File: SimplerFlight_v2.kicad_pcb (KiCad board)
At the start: 2 copper layers, 77 parts, among them J1 Battery 1, J10 Cam 2, J11 Cam 3, J12 Encoder, J13 Servo, J14 DM3CS-SF, J3 USART1 Header, J4 I2C1 Header, J5 SPI Header, J6 SWD Header, J7 Battery 2, J8 USB, J9 Cam 1, SW1 Boot Switch, SW2 System Reset, U1 AMS1117-3.3, U2 STM32F401RETx, U3 BMP581, U4 BNO085, U5 TPS62933, U6 TPS62933, U7 W25X40CLSNIG, Y1 16MHz, Y2 Crystal

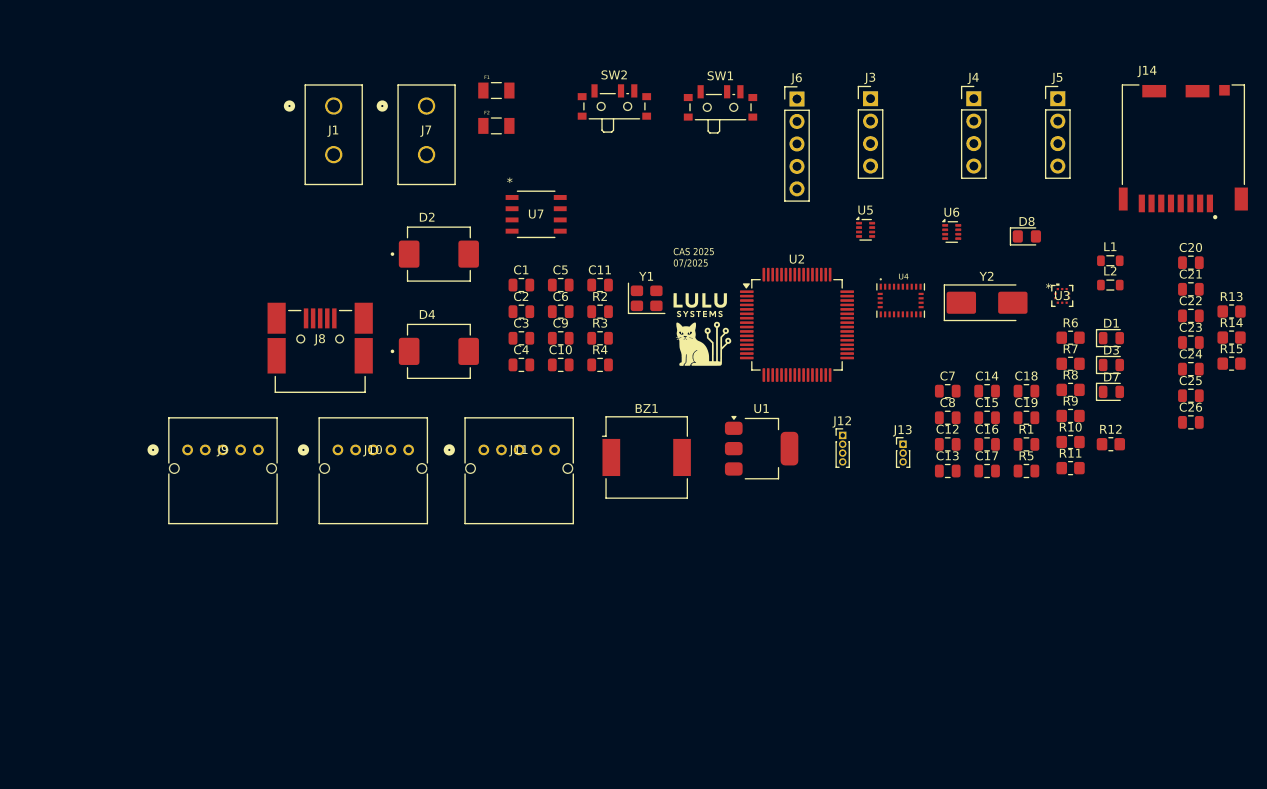
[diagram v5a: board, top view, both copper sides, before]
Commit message: Update schematic, pending power sims, updated README
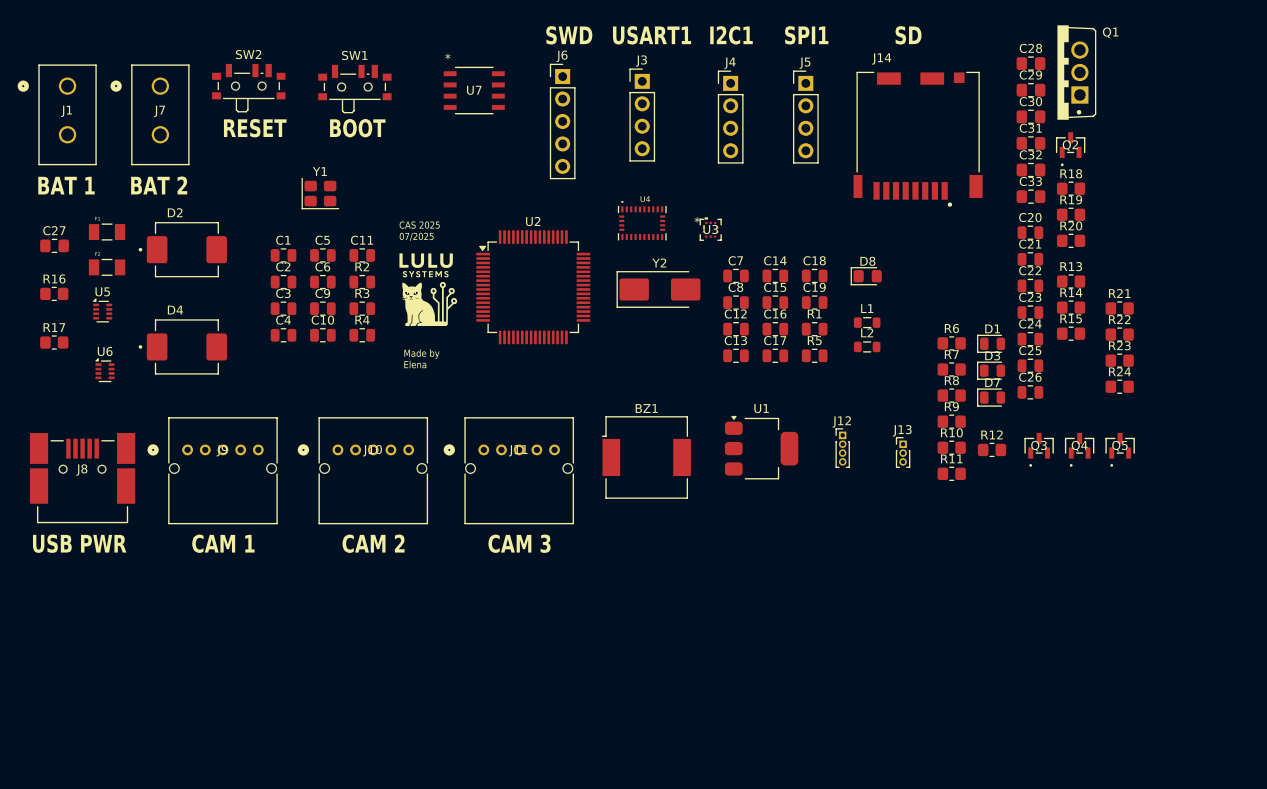
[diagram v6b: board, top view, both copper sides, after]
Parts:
- added C27: 100nF, Capacitor_SMD:C_0805_2012Metric_Pad1.18x1.45mm_HandSolder, F.Cu at (52.0, 40.6)
- added C28: 10uF, Capacitor_SMD:C_0805_2012Metric_Pad1.18x1.45mm_HandSolder, F.Cu at (162.5, 19.9)
- added C29: 100uF, Capacitor_SMD:C_0805_2012Metric_Pad1.18x1.45mm_HandSolder, F.Cu at (162.5, 23.0)
- added C30: 100uF, Capacitor_SMD:C_0805_2012Metric_Pad1.18x1.45mm_HandSolder, F.Cu at (162.5, 26.0)
- added C31: 10uF, Capacitor_SMD:C_0805_2012Metric_Pad1.18x1.45mm_HandSolder, F.Cu at (162.5, 29.0)
- added C32: 100uF, Capacitor_SMD:C_0805_2012Metric_Pad1.18x1.45mm_HandSolder, F.Cu at (162.5, 32.0)
- added C33: 10uF, Capacitor_SMD:C_0805_2012Metric_Pad1.18x1.45mm_HandSolder, F.Cu at (162.5, 35.0)
- added Q1: IRF520NPBF, IRF520NPBF:TO-220-3, F.Cu at (168.0, 21.0)
- added Q2: NPN, FSB560A:SSOT3_3X1P5_ONS, F.Cu at (167.0, 29.2)
- added Q3: NPN, FSB560A:SSOT3_3X1P5_ONS, F.Cu at (163.4, 63.2)
- added Q4: NPN, FSB560A:SSOT3_3X1P5_ONS, F.Cu at (168.0, 63.2)
- added Q5: NPN, FSB560A:SSOT3_3X1P5_ONS, F.Cu at (172.5, 63.2)
- added R16: 10k, Resistor_SMD:R_0805_2012Metric_Pad1.20x1.40mm_HandSolder, F.Cu at (52.0, 46.0)
- added R17: 10k, Resistor_SMD:R_0805_2012Metric_Pad1.20x1.40mm_HandSolder, F.Cu at (52.0, 51.5)
- added R18: 10K, Resistor_SMD:R_0805_2012Metric_Pad1.20x1.40mm_HandSolder, F.Cu at (167.0, 34.1)
- added R19: 10k, Resistor_SMD:R_0805_2012Metric_Pad1.20x1.40mm_HandSolder, F.Cu at (167.0, 37.0)
- added R20: 470, Resistor_SMD:R_0805_2012Metric_Pad1.20x1.40mm_HandSolder, F.Cu at (167.0, 40.0)
- added R21: R, Resistor_SMD:R_0805_2012Metric_Pad1.20x1.40mm_HandSolder, F.Cu at (172.5, 47.6)
- added R22: R, Resistor_SMD:R_0805_2012Metric_Pad1.20x1.40mm_HandSolder, F.Cu at (172.5, 50.6)
- added R23: R, Resistor_SMD:R_0805_2012Metric_Pad1.20x1.40mm_HandSolder, F.Cu at (172.5, 53.5)
- added R24: R, Resistor_SMD:R_0805_2012Metric_Pad1.20x1.40mm_HandSolder, F.Cu at (172.5, 56.5)
- moved U6 97.0 mm to (57.7, 54.8)
- moved U5 86.8 mm to (57.5, 48.0)
- moved F1 46.8 mm to (58.0, 39.0)
- moved F2 46.8 mm to (58.0, 43.0)
- moved SW1 41.4 mm to (86.0, 22.3)
- moved SW2 41.4 mm to (74.0, 22.2)
- moved U3 40.5 mm to (126.2, 38.8)
- moved Y1 38.8 mm to (82.1, 34.6)
- moved Y2 37.0 mm to (120.5, 45.5)
- moved G*** 31.3 mm to (94.0, 45.5)
- moved J8 30.6 mm to (55.2, 65.8)
- moved U4 30.5 mm to (118.5, 38.0)
- moved J1 30.2 mm to (53.5, 22.5)
- moved J7 30.2 mm to (64.0, 22.5)
- moved U2 30.1 mm to (106.2, 45.2)
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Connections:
- net Net-(D8-A) renamed /Power/VBUS_CAM
- net Net-(D8-K) renamed /Power/VBUS_USB
- net Net-(U5-VIN) renamed /Power/VBUS_SERVO
- BZ1 pad 1: unconnected-(BZ1-+-Pad1) -> +3V3
- BZ1 pad 2: unconnected-(BZ1---Pad2) -> Net-(BZ1--)
- J10 pad 1: unconnected-(J10-Pad1) -> Net-(Q4-E)
- J10 pad 2: unconnected-(J10-Pad2) -> GND
- J10 pad 3: unconnected-(J10-Pad3) -> CAM2_RX
- J10 pad 4: unconnected-(J10-Pad4) -> CAM2_TX
- J11 pad 1: unconnected-(J11-Pad1) -> Net-(Q3-E)
- J11 pad 2: unconnected-(J11-Pad2) -> GND
- J11 pad 3: unconnected-(J11-Pad3) -> CAM3_RX
- J11 pad 4: unconnected-(J11-Pad4) -> CAM3_TX
- J12 pad 1: unconnected-(J12-Pin_1-Pad1) -> 5V_SERVO
- J12 pad 2: unconnected-(J12-Pin_2-Pad2) -> GND
- J12 pad 3: unconnected-(J12-Pin_3-Pad3) -> ENC_A
- J12 pad 4: unconnected-(J12-Pin_4-Pad4) -> ENC_B
- J13 pad 1: unconnected-(J13-Pin_1-Pad1) -> SERVO_PWM
- J13 pad 2: unconnected-(J13-Pin_2-Pad2) -> Net-(J13-Pin_2)
- J13 pad 3: unconnected-(J13-Pin_3-Pad3) -> GND
- J14 pad 2: unconnected-(J14-CD/DAT3-Pad2) -> CS
- J14 pad 3: unconnected-(J14-CMD-Pad3) -> SI
- J14 pad 4: unconnected-(J14-VDD-Pad4) -> +3V3
- J14 pad 5: unconnected-(J14-CLK-Pad5) -> SCK
- J14 pad 6: unconnected-(J14-VSS-Pad6) -> GND
- J14 pad 7: unconnected-(J14-DAT0-Pad7) -> SO
- J14 pad 9: unconnected-(J14-CD_SW-Pad9) -> C_DET
- J14 pad S1: unconnected-(J14-GND-PadS1) -> GND
- J14 pad S2: unconnected-(J14-GND__1-PadS2) -> GND
- J14 pad S3: unconnected-(J14-GND__2-PadS3) -> GND
- J14 pad S5: unconnected-(J14-GND__3-PadS5) -> GND
- J8 pad 2: /Power/USB_OTG_FS_D- -> USB_DN
- J8 pad 3: /Power/USB_OTG_FS_D+ -> USB_DP
- J9 pad 1: unconnected-(J9-Pad1) -> Net-(Q5-E)
- J9 pad 2: unconnected-(J9-Pad2) -> GND
- J9 pad 3: unconnected-(J9-Pad3) -> CAM1_RX
- J9 pad 4: unconnected-(J9-Pad4) -> CAM1_TX
- U2 pad 44: /Microcontroller/USB_OTG_FS_D- -> USB_DN
- U2 pad 45: /Microcontroller/USB_OTG_FS_D+ -> USB_DP
- U5 pad 2: unconnected-(U5-EN-Pad2) -> Net-(U5-EN)
- U5 pad 4: unconnected-(U5-GND-Pad4) -> GND
- U6 pad 2: unconnected-(U6-EN-Pad2) -> Net-(U6-EN)
- U6 pad 4: unconnected-(U6-GND-Pad4) -> GND
- U7 pad 4: unconnected-(U7-GND-Pad4) -> GND
- U7 pad 8: unconnected-(U7-VCC-Pad8) -> +3V3
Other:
- board text added: "BAT 1"
- board text added: "BAT 2"
- board text added: "BOOT"
- board text added: "CAM 1"
- board text added: "CAM 2"
- board text added: "CAM 3"
- board text added: "I2C1"
- board text added: "Made by Elena"
- board text added: "RESET"
- board text added: "SD"
- board text added: "SPI1"
- board text added: "SWD"
- board text added: "USART1"
- board text added: "USB PWR"

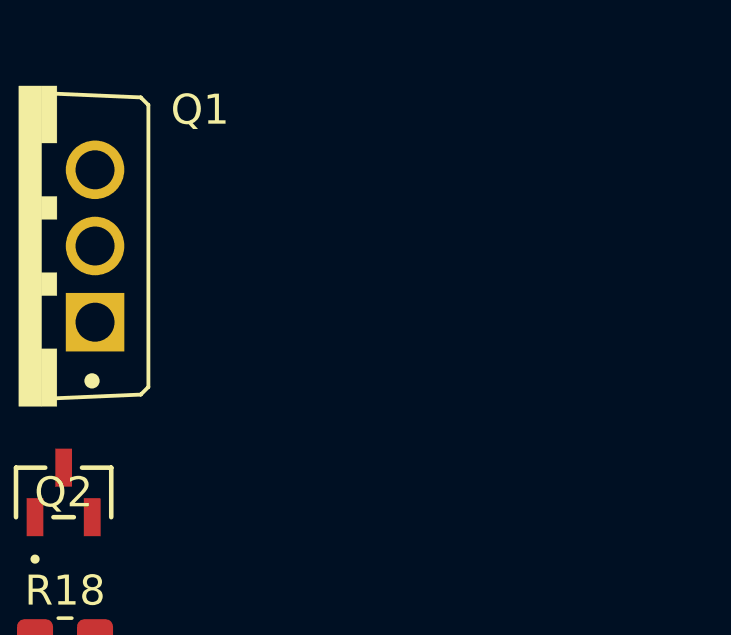
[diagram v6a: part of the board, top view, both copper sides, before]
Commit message: Remove transistor enable for servo power. Added falstad sim files
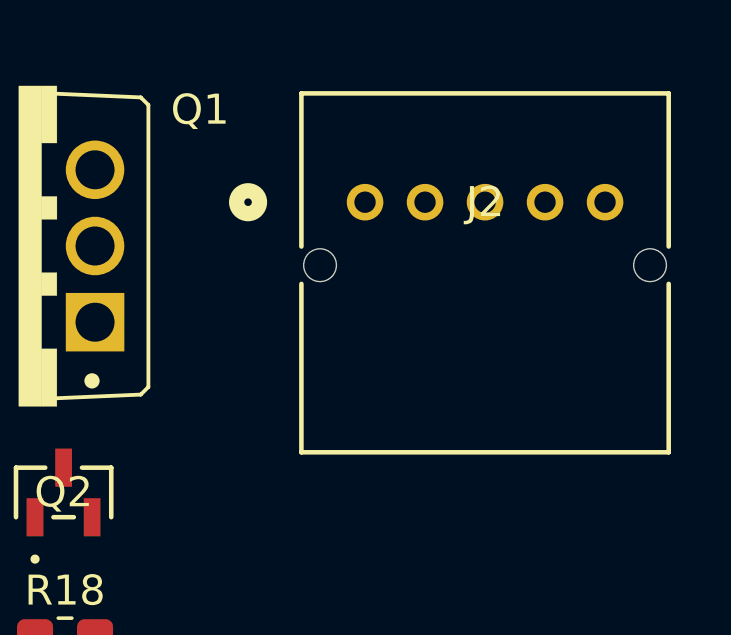
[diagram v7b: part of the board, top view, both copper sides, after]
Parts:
- added J2: Encoder, S05B_PASK_2_LF__SN_:CONN_S05B-PASK-2_JST, F.Cu at (177.0, 19.5)
- R21, R23: value R -> 25R
- R22, R24: value R -> 5R
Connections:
- net Net-(U5-EN) renamed /Power/U5_VEN
- net Net-(U6-EN) renamed /Power/U6_VEN

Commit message: Updated schematics
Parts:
- added G***: LOGO, LOGO, F.Cu at (94.9, 33.5)
